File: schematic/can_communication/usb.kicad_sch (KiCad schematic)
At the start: 2 parts, among them J1 USB_C_Receptacle_USB2.0_16P, U2 USBLC6-2SC6

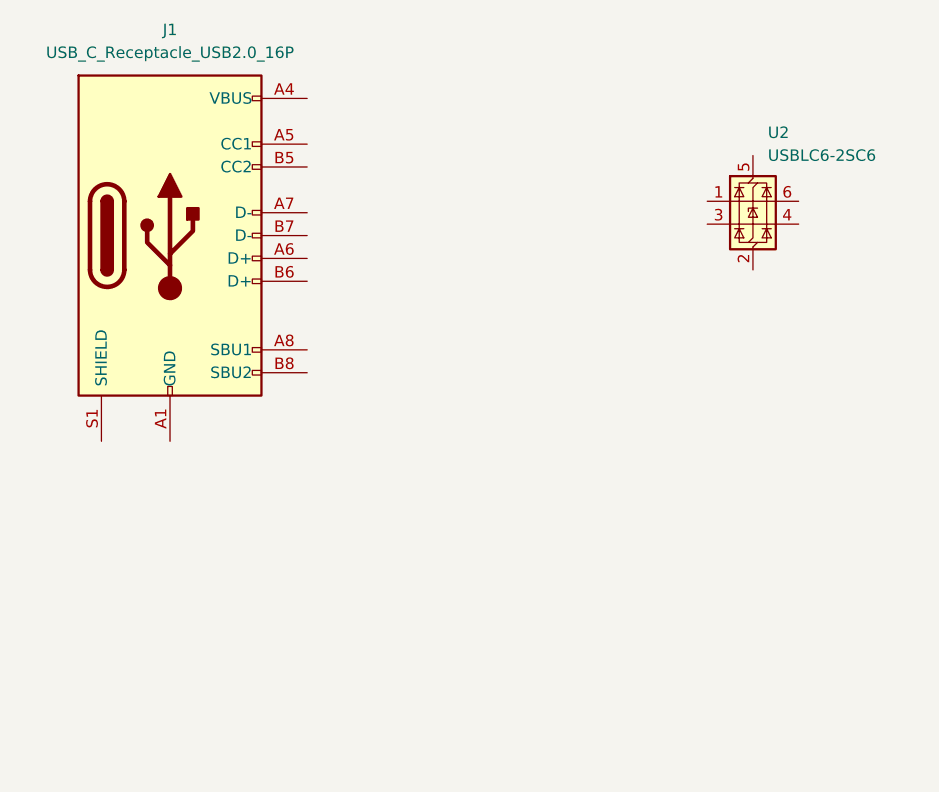
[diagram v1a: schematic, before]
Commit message: added usb device specifics
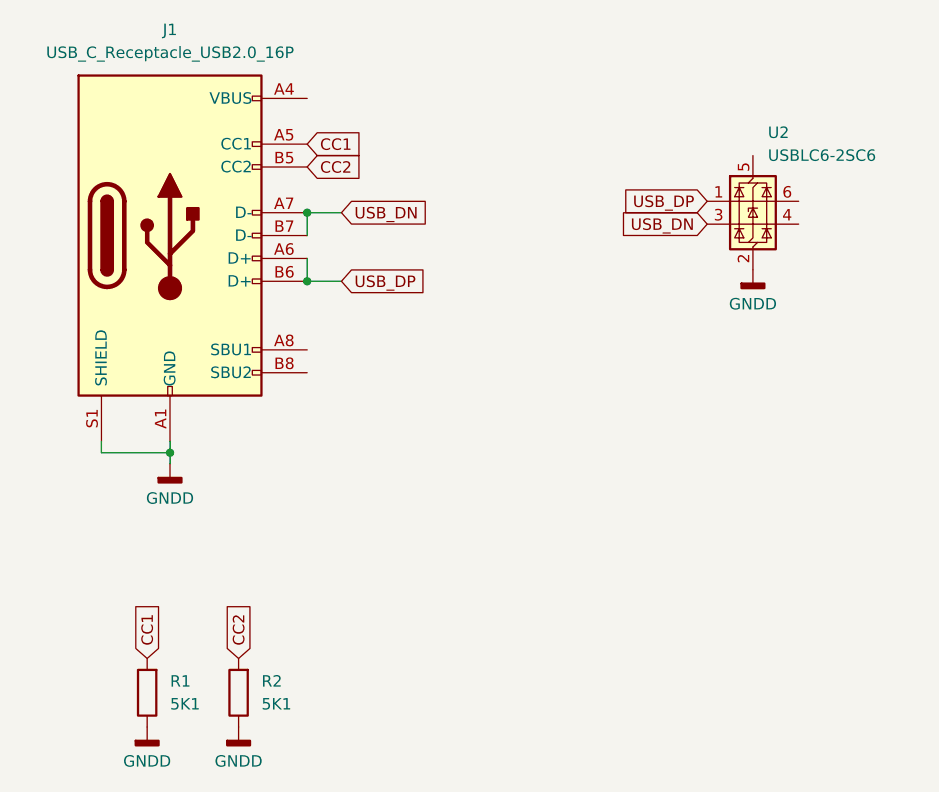
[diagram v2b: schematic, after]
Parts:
- added R1, R2: 5K1, symbol Device:R
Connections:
- net GNDD: now reaches J1.A1 (GND), J1.A12 (GND), J1.B1 (GND), J1.B12 (GND)
- net GNDD: now also J1.S1 (SHIELD), U2.2 (GND), R1.1, R2.1
- net CC1: now reaches J1.A5 (CC1)
- net CC1: now also R1.2
- net USB_DP: now reaches J1.A6 (D+)
- net USB_DP: now also J1.B6 (D+), U2.1 (I/O1)
- net USB_DN: now reaches J1.A7 (D-)
- net USB_DN: now also J1.B7 (D-), U2.3 (I/O2)
- net CC2: now reaches J1.B5 (CC2)
- net CC2: now also R2.2

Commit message: added neccessary connection for stm32h7
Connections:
- net USB_VBUS: now reaches J1.A4 (VBUS), J1.A9 (VBUS), J1.B4 (VBUS), J1.B9 (VBUS)
- net USB_VBUS: now also U2.5 (VBUS)
- net USB_DN_P: now reaches U2.4 (I/O2)
- net USB_DP_P: now reaches U2.6 (I/O1)
- no-connect marks 0 -> 2
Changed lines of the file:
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@@
 		(color 0 0 0 0)
 	)
+	(no_connect
+		(at 90.17 96.52)
+	)
+	(no_connect
+		(at 90.17 99.06)
+	)
 	(wire
 		(pts
@@
 		)
 	)
+	(global_label "USB_DN_P"
+		(shape input)
+		(at 144.78 82.55 0)
+		(fields_autoplaced yes)
+		(effects
+			(font
+				(size 1.27 1.27)
+			)
+			(justify left)
+		)
+		(property "Intersheetrefs" "${INTERSHEET_REFS}"
+			(at 157.3809 82.55 0)
+			(effects
+				(font
+					(size 1.27 1.27)
+				)
+				(justify left)
+				(hide yes)
+			)
+		)
+	)
 	(global_label "USB_DN"
 		(shape input)
@@
 		)
 	)
+	(global_label "USB_VBUS"
+		(shape input)
+		(at 139.7 74.93 90)
+		(fields_autoplaced yes)
+		(effects
+			(font
+				(size 1.27 1.27)
+			)
+			(justify left)
+		)
+		(property "Intersheetrefs" "${INTERSHEET_REFS}"
+			(at 139.7 62.2686 90)
+			(effects
+				(font
+					(size 1.27 1.27)
+				)
+				(justify left)
+				(hide yes)
+			)
+		)
+	)
+	(global_label "USB_DP_P"
+		(shape input)
+		(at 144.78 80.01 0)
+		(fields_autoplaced yes)
+		(effects
+			(font
+				(size 1.27 1.27)
+			)
+			(justify left)
+		)
+		(property "Intersheetrefs" "${INTERSHEET_REFS}"
+			(at 157.3204 80.01 0)
+			(effects
+				(font
+					(size 1.27 1.27)
+				)
+				(justify left)
+				(hide yes)
+			)
+		)
+	)
 	(global_label "USB_DP"
 		(shape input)
@@
 				(hide yes)
 			)
+		)
+	)
+	(global_label "USB_VBUS"
+		(shape input)
+		(at 90.17 68.58 0)
+		(fields_autoplaced yes)
+		(effects
+			(font
+				(size 1.27 1.27)
+			)
+			(justify left)
+		)
+		(property "Intersheetrefs" "${INTERSHEET_REFS}"
+			(at 102.8314 68.58 0)
+			(effects
+				(font
+					(size 1.27 1.27)
+				)
+				(justify left)
+				(hide yes)
+			)
